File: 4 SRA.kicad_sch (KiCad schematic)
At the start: 38 parts, among them J1 USB_B_Micro, J6 Conn_01x18_Pin, J7 Conn_01x18_Pin, Q1 SS8050, Q2 SS8050, SW1 SW_Push, SW2 SW_Push, U1 CP2102N-Axx-xQFN28, U2 AMS1117-3.3, U4 ESP32-WROOM-32D

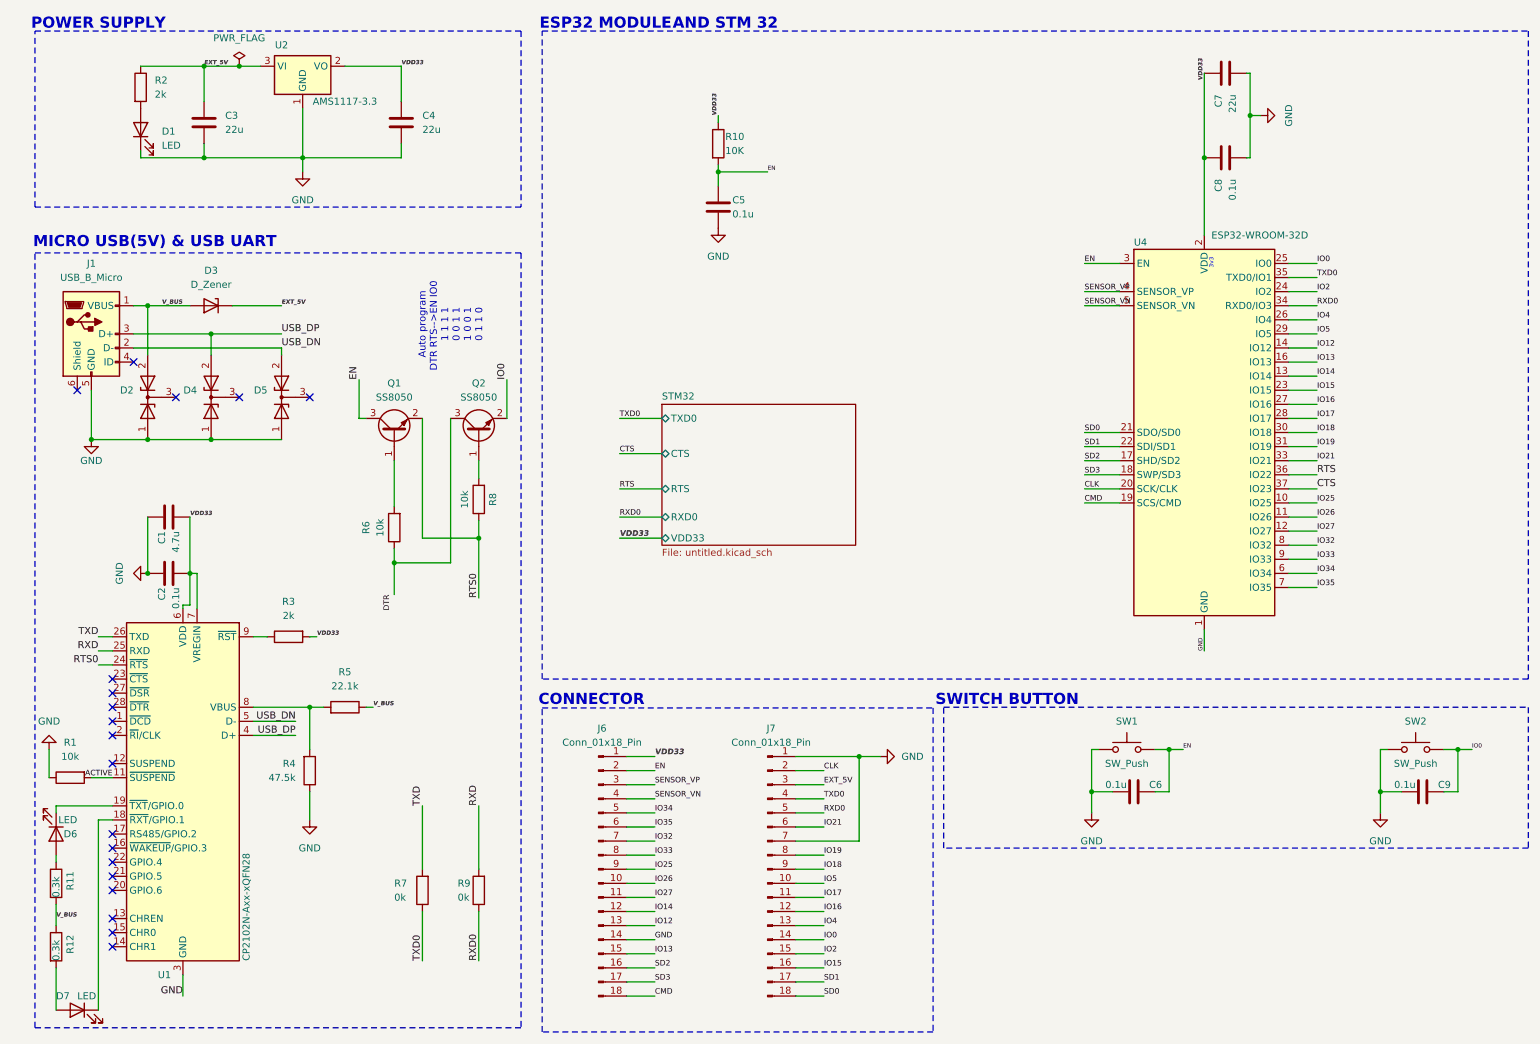
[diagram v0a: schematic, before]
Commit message: issues solved!!
Streamlined the design by resolving CP2102N and ESP32 TX/RX pin issues. All necessary footprints were assigned, favoring 0805 SMD components for a compact board layout
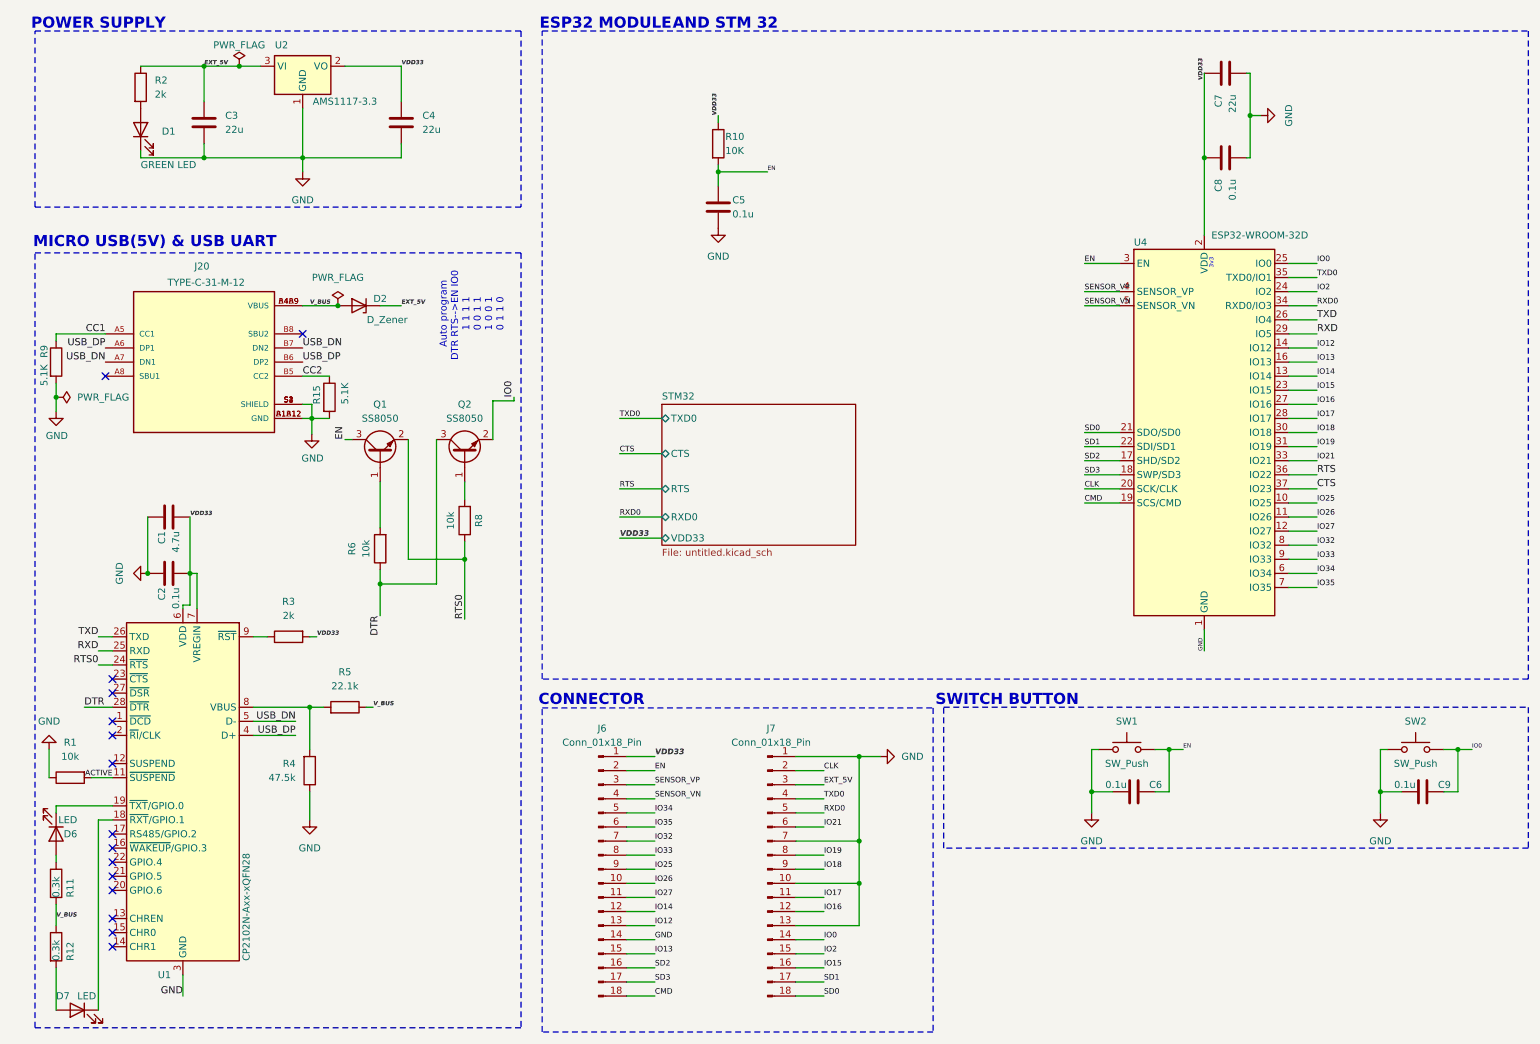
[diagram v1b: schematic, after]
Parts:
- removed D2, D4, D5: D_Zener_Dual_CommonCathode_AAK, symbol Device:D_Zener_Dual_CommonCathode_AAK
- removed D3: D_Zener, symbol Device:D_Zener
- removed J1: USB_B_Micro, symbol Connector:USB_B_Micro
- removed R7, R9: 0k, symbol Device:R
- added D2: D_Zener, Diode_SMD:D_0805_2012Metric_Pad1.15x1.40mm_HandSolder, symbol Device:D_Zener
- added J20: TYPE-C-31-M-12, Connector_USB:USB_C_Receptacle_HRO_TYPE-C-31-M-12, symbol ESP32-S2-rescue:TYPE-C-31-M-12-TYPE-C-31-M-12
- added R15, R9: 5.1K, Resistor_SMD:R_0805_2012Metric, symbol ESP32-S2-rescue:R-Device
- C1, C2, C3, C4, C5, C6, C7, C8, C9: footprint (none) -> Capacitor_SMD:C_0805_2012Metric_Pad1.18x1.45mm_HandSolder
- D1: value LED -> GREEN LED; footprint (none) -> LED_SMD:LED_0805_2012Metric_Pad1.15x1.40mm_HandSolder
- D6, D7: footprint (none) -> LED_SMD:LED_0805_2012Metric_Pad1.15x1.40mm_HandSolder
- J6, J7: footprint (none) -> Connector_PinHeader_2.54mm:PinHeader_1x18_P2.54mm_Vertical
- R1, R10, R11, R12, R2, R3, R4, R5, R6, R8: footprint (none) -> Resistor_SMD:R_0805_2012Metric_Pad1.20x1.40mm_HandSolder
- SW1, SW2: footprint (none) -> Button_Switch_SMD:SW_Push_1P1T_NO_CK_KSC6xxJ
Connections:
- net ^{DTR} is gone; now on net DTR: Q2.3 (C), R6.1
- net EXT_5V: now also D2.1 (K)
- net GND: now also J7.10 (Pin_10), J7.13 (Pin_13), J20.A1B12 (GND), J20.B1A12 (GND), J20.S1 (SHIELD), J20.S2 (SHIELD), J20.S3 (SHIELD), J20.S4 (SHIELD), R15.2, R9.2
- net RXD: now also U4.29 (IO5)
- net TXD: now also U4.26 (IO4)
- net USB_DN: now also J20.A7 (DN1), J20.B7 (DN2)
- net USB_DP: now also J20.A6 (DP1), J20.B6 (DP2)
- net V_BUS: now also D2.2 (A), J20.A4B9 (VBUS), J20.B4A9 (VBUS)
- net DTR: now reaches U1.28 (~{DTR})
- removed net IO4: J7.13 (Pin_13), U4.26 (IO4)
- removed net IO5: J7.10 (Pin_10), U4.29 (IO5)
- new net CC1: J20.A5 (CC1), R9.1
- new net CC2: J20.B5 (CC2), R15.1
- no-connect marks 19 -> 15
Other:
- moved on the sheet: Q1, Q2, R6, R8

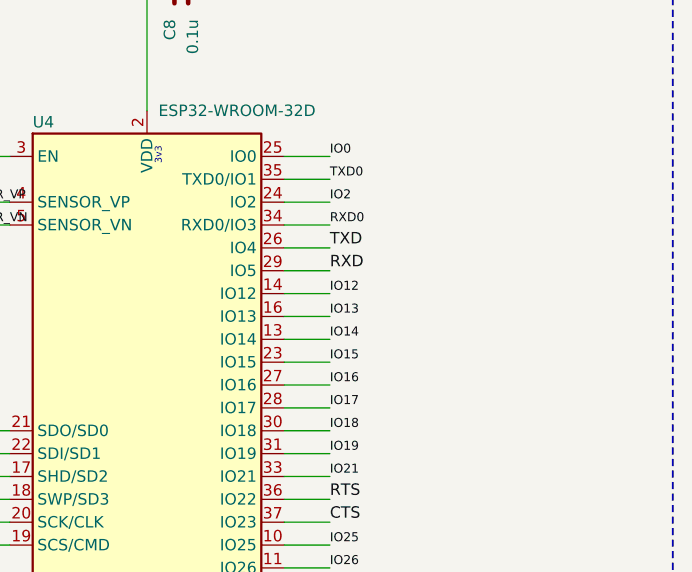
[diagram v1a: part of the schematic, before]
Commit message: Battery System Integration Complete
Added comprehensive battery functionality to the development board, including integrated battery protection circuitry and USB-C charging capability. All schematics have been updated to reflect the new power management topology and charging infrastructure
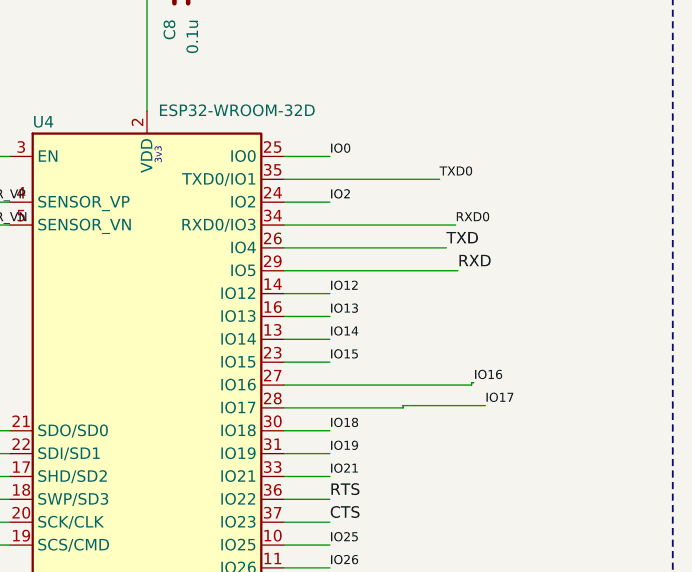
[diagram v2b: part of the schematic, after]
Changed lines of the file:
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@@
+	(wire
+		(pts
+			(xy 257.302 62.23) (xy 240.03 62.23)
+		)
+		(stroke
+			(width 0)
+			(type default)
+		)
+	)
 	(wire
 		(pts
@@
 	(wire
 		(pts
-			(xy 240.03 72.39) (xy 245.11 72.39)
+			(xy 240.03 72.39) (xy 259.334 72.39)
 		)
 		(stroke
@@
 	(wire
 		(pts
+			(xy 253.238 87.376) (xy 253.238 87.63)
+		)
+		(stroke
+			(width 0)
+			(type default)
+		)
+	)
+	(wire
+		(pts
 			(xy 151.13 189.23) (xy 156.21 189.23)
 		)
@@
 	(wire
 		(pts
+			(xy 260.858 84.836) (xy 260.858 85.09)
+		)
+		(stroke
+			(width 0)
+			(type default)
+		)
+	)
+	(wire
+		(pts
 			(xy 120.65 191.77) (xy 125.73 191.77)
 		)
@@
 	(wire
 		(pts
-			(xy 240.03 67.31) (xy 245.11 67.31)
+			(xy 240.03 67.31) (xy 259.08 67.31)
 		)
 		(stroke
@@
 	(wire
 		(pts
+			(xy 253.238 87.63) (xy 240.03 87.63)
+		)
+		(stroke
+			(width 0)
+			(type default)
+		)
+	)
+	(wire
+		(pts
 			(xy 224.79 125.73) (xy 224.79 129.54)
 		)
@@
 	(wire
 		(pts
-			(xy 240.03 85.09) (xy 245.11 85.09)
+			(xy 260.858 84.836) (xy 261.112 84.836)
 		)
 		(stroke
@@
 	(wire
 		(pts
+			(xy 260.858 85.09) (xy 240.03 85.09)
+		)
+		(stroke
+			(width 0)
+			(type default)
+		)
+	)
+	(wire
+		(pts
 			(xy 218.44 154.94) (xy 215.9 154.94)
 		)
@@
 	(wire
 		(pts
-			(xy 240.03 69.85) (xy 245.11 69.85)
+			(xy 240.03 69.85) (xy 258.064 69.85)
 		)
 		(stroke
@@
 	(wire
 		(pts
-			(xy 240.03 87.63) (xy 245.11 87.63)
+			(xy 253.238 87.376) (xy 262.382 87.376)
 		)
 		(stroke
@@
 		(pts
 			(xy 62.23 85.09) (xy 63.881 85.09)
-		)
-		(stroke
-			(width 0)
-			(type default)
-		)
-	)
-	(wire
-		(pts
-			(xy 240.03 62.23) (xy 245.11 62.23)
 		)
 		(stroke
@@
 	)
 	(label "TXD0"
-		(at 245.11 62.23 0)
+		(at 257.302 62.23 0)
 		(effects
 			(font
@@
 	)
 	(label "TXD"
-		(at 245.11 69.85 0)
+		(at 258.064 69.85 0)
 		(effects
 			(font
@@
 	)
 	(label "RXD0"
-		(at 245.11 67.31 0)
+		(at 259.08 67.31 0)
 		(effects
 			(font
@@
 	)
 	(label "IO16"
-		(at 245.11 85.09 0)
+		(at 261.112 84.836 0)
 		(effects
 			(font
@@
 	)
 	(label "IO17"
-		(at 245.11 87.63 0)
+		(at 262.382 87.376 0)
 		(effects
 			(font
@@
 	)
 	(label "RXD"
-		(at 245.11 72.39 0)
-		(effects
-			(font
+		(at 259.334 72.39 0)
+		(effects
+			(font
